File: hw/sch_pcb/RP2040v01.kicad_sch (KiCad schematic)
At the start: 46 parts, among them J1 HEADER_1x03, J2 USBC_USB4105-GF-A, J3 HEADER_1x03, J4 HEADER_1x10, J5 HEADER_1x10, J6 HEADER_1x10, J7 HEADER_1x10, J8 HEADER_2x05, Q1 BC817-25, SW1 434133025816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

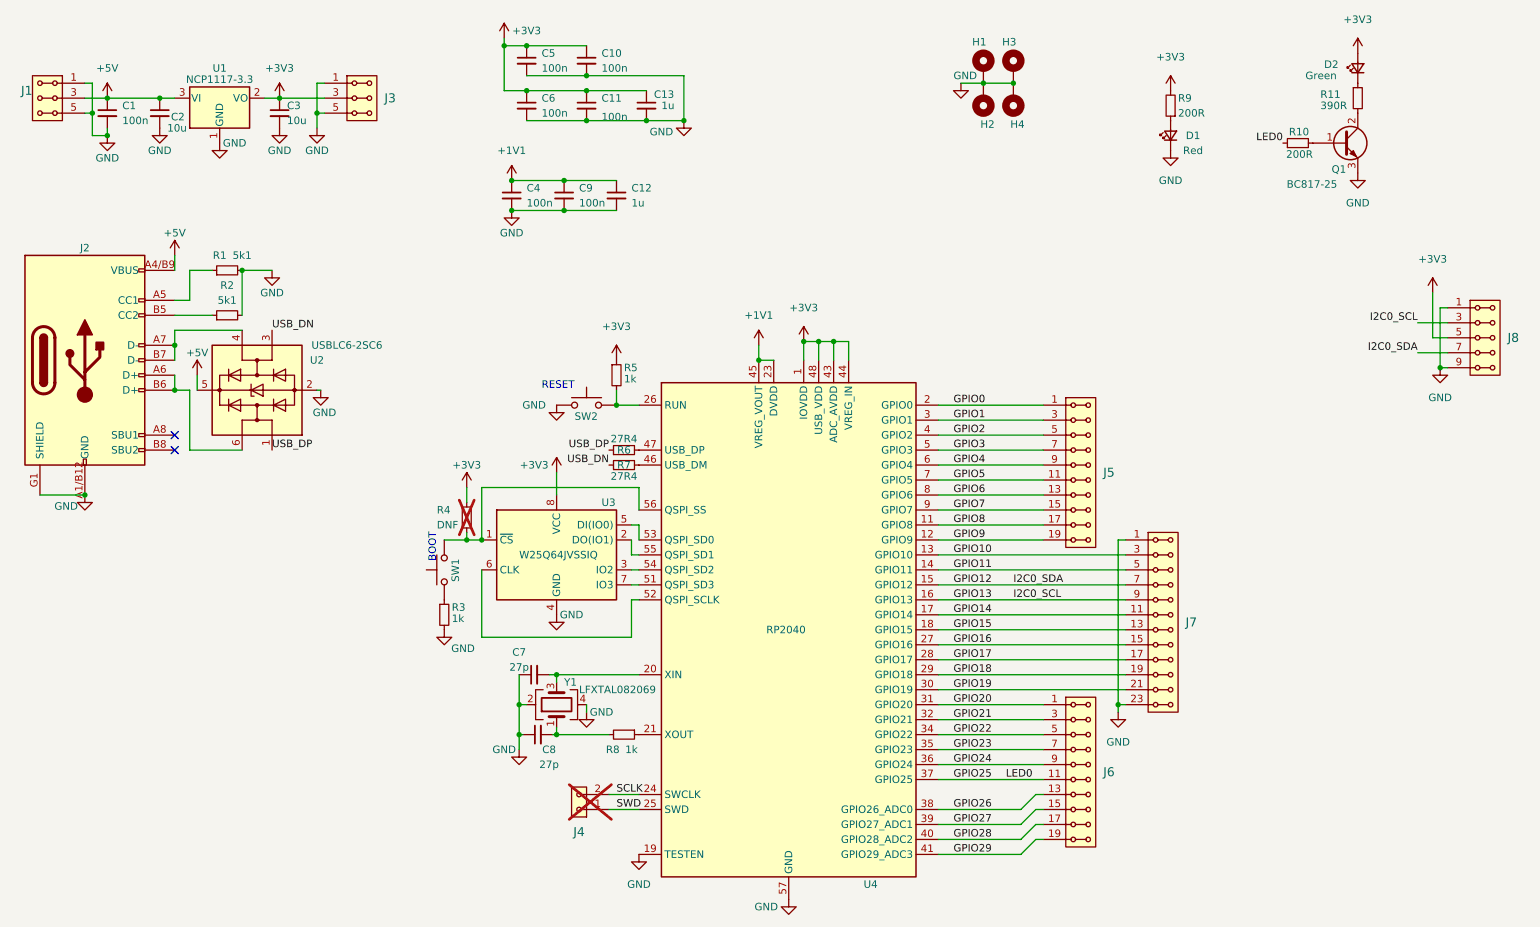
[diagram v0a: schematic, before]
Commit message: Update project to KiCADv9.
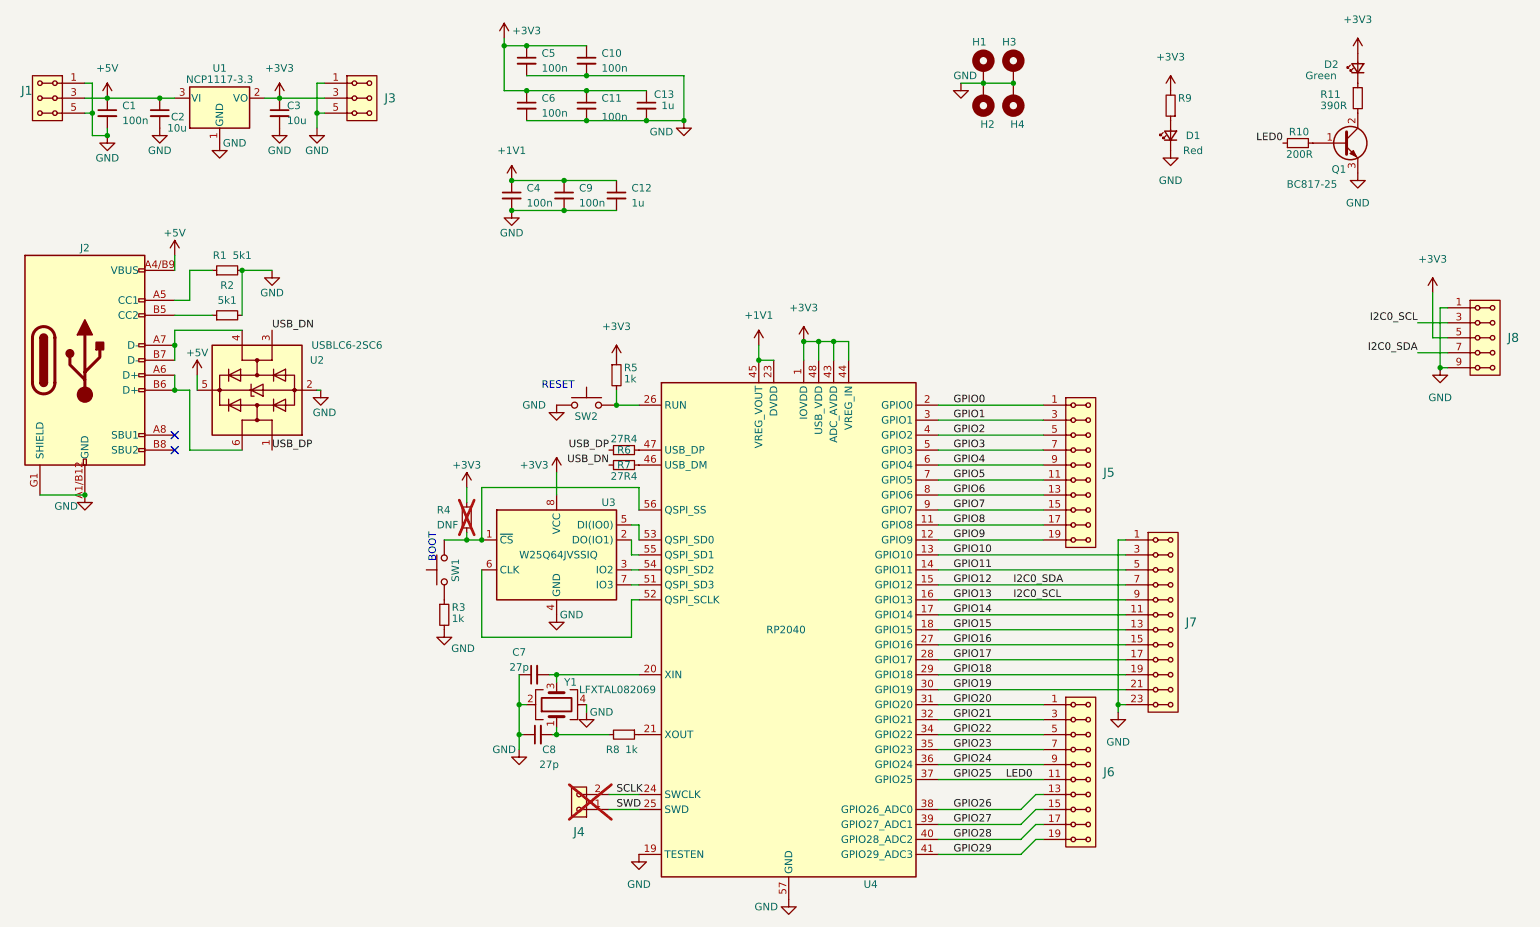
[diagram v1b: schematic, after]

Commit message: Cleanup Fab layer.
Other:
- company: (none) -> Mlab.cz
- title: (none) -> RP2040v01A
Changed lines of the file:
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@@
 	(generator_version "9.0")
 	(paper "A4")
+	(title_block
+		(title "RP2040v01A")
+		(company "Mlab.cz")
+		(comment 1 "MCU board for RP2040 dual-core microcontroller.")
+	)
 	(text "BOOT"
 		(exclude_from_sim no)
